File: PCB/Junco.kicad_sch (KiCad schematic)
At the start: 206 parts, among them J1 AudioJack4, J2 AudioJack4, SW1 SW_Push, SW10 SW_Push, SW11 SW_Push, SW12 SW_Push, SW13 SW_Push, SW14 SW_Push, SW15 SW_Push, SW16 SW_Push, SW17 SW_Push, SW18 SW_Push, SW19 SW_MX_Hotswap_Rotary_Switch_R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, SW2 SW_Push, SW20 SW_Push, SW21 SW_Push, SW22 SW_Push, SW23 SW_Push, SW24 SW_Push, SW25 SW_Push, SW26 SW_Push, SW27 SW_Push, SW28 SW_Push, SW29 SW_Push, SW3 SW_Push, SW30 RotaryEncoder_Switch, SW31 SW_Push, SW32 SW_Push, SW33 SW_Push, SW34 SW_Push, SW35 SW_Push, SW36 SW_Push, SW37 SW_Push, SW38 SW_Push, SW39 SW_Push, SW4 SW_Push, SW40 SW_Push, SW41 SW_Push, SW42 SW_Push, SW43 SW_Push, SW44 SW_Push, SW45 SW_Push, SW46 SW_Push, SW47 SW_Push, SW48 SW_Push, SW49 SW_MX_Hotswap_Rotary_Switch_R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, SW5 SW_Push, SW50 SW_Push, SW51 SW_Push, SW52 SW_Push, SW53 SW_Push, SW54 SW_Push, SW55 SW_Push, SW56 SW_Push, SW57 SW_Push, SW58 SW_Push, SW59 SW_Push, SW6 SW_Push, SW60 RotaryEncoder_Switch, SW7 SW_Push, SW8 SW_Push, SW9 SW_Push, U1 Pico, U2 SN74AHCT1G125, U3 Pico, U4 SN74AHCT1G125

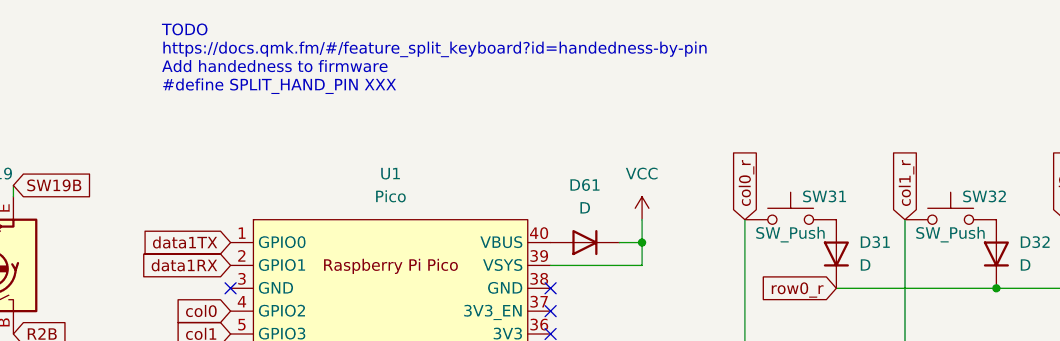
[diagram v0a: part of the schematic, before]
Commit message: Added JLC part number to LED and switch symbols
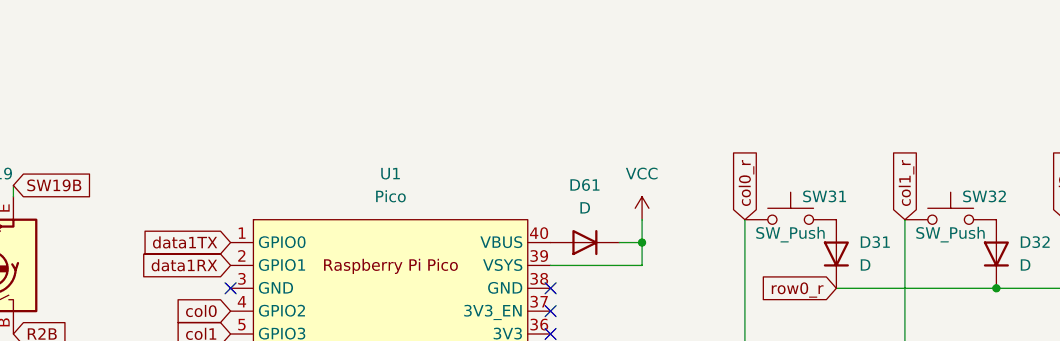
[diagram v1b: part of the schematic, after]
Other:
- note removed: "TODO https://docs.qmk.fm/#/feature_split_keyboard?id=handedness-by-pin Add handedness to firmware #define SPLIT_HAND_PIN XXX"

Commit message: Added level shifter bypass jumper Schematic updated Symbol created and placed
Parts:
- added JP1, JP2: Level shifter bypass jumper, Junco:Level Shifter Bypass Jumper, symbol Jumper:SolderJumper_2_Open
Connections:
- net led: now also JP1.1 (A)
- net led_r: now also JP2.1 (A)
- net at SK68XX_Mini38.4 (DIN), U4.4 (DOUT): now also JP2.2 (B)
- net at SK68XX_Mini1.4 (DIN), U2.4 (DOUT): now also JP1.2 (B)
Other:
- moved on the sheet: SK68XX_Mini1, SK68XX_Mini10, SK68XX_Mini11, SK68XX_Mini12, SK68XX_Mini13, SK68XX_Mini14, SK68XX_Mini15, SK68XX_Mini16, SK68XX_Mini17, SK68XX_Mini18, SK68XX_Mini19, SK68XX_Mini2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

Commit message: Consolidated LED footprints
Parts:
- SK68XX_Mini1, SK68XX_Mini2, SK68XX_Mini3, SK68XX_Mini38, SK68XX_Mini39, SK68XX_Mini4, SK68XX_Mini40, SK68XX_Mini41, SK68XX_Mini42, SK68XX_Mini43, SK68XX_Mini44, SK68XX_Mini45, SK68XX_Mini5, SK68XX_Mini6, SK68XX_Mini7, SK68XX_Mini8: value SK68XXMini -> SK6803MINI-E
- SK68XX_Mini10, SK68XX_Mini11, SK68XX_Mini12, SK68XX_Mini13, SK68XX_Mini14, SK68XX_Mini15, SK68XX_Mini16, SK68XX_Mini17, SK68XX_Mini18, SK68XX_Mini19, SK68XX_Mini20, SK68XX_Mini21, SK68XX_Mini22, SK68XX_Mini23, SK68XX_Mini24, SK68XX_Mini25, SK68XX_Mini26, SK68XX_Mini28, SK68XX_Mini29, SK68XX_Mini30, SK68XX_Mini31, SK68XX_Mini32, SK68XX_Mini33, SK68XX_Mini34, SK68XX_Mini35, SK68XX_Mini36, SK68XX_Mini37, SK68XX_Mini46, SK68XX_Mini47, SK68XX_Mini48, SK68XX_Mini49, SK68XX_Mini50, SK68XX_Mini51, SK68XX_Mini52, SK68XX_Mini53, SK68XX_Mini54, SK68XX_Mini55, SK68XX_Mini56, SK68XX_Mini57, SK68XX_Mini58, SK68XX_Mini59, SK68XX_Mini60, SK68XX_Mini61, SK68XX_Mini62, SK68XX_Mini63, SK68XX_Mini65, SK68XX_Mini66, SK68XX_Mini67, SK68XX_Mini68, SK68XX_Mini69, SK68XX_Mini70, SK68XX_Mini71, SK68XX_Mini72, SK68XX_Mini73, SK68XX_Mini74, SK68XX_Mini9: footprint Junco:SK68XXMini_Offset -> Junco:SK68XXMini
- SK68XX_Mini27: value SK68XXMini_Short_Offset_for_Rotary_Encoder -> SK6803MINI-E; footprint Junco:SK68XXMini_Short_Offset_for_Rotary_Encoder -> Junco:SK68XXMini
- SK68XX_Mini64: value SK68XXMini -> SK6803MINI-E; footprint Junco:SK68XXMini_Short_Offset_for_Rotary_Encoder -> Junco:SK68XXMini
- SW19, SW49: value SW_MX_Hotswap_Rotary_Switch_Rotated -> SW_MX_Hotswap_Rotary_Switch; footprint Junco:SW_MX_Hotswap_Rotary_Switch_Rotated -> Junco:SW_MX_Hotswap_Rotary_Switch

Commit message: Consolidated Switch footprints with 1.5u and 1u
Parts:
- SK68XX_Mini10, SK68XX_Mini11, SK68XX_Mini12, SK68XX_Mini13, SK68XX_Mini14, SK68XX_Mini15, SK68XX_Mini16, SK68XX_Mini17, SK68XX_Mini18, SK68XX_Mini19, SK68XX_Mini20, SK68XX_Mini21, SK68XX_Mini22, SK68XX_Mini23, SK68XX_Mini24, SK68XX_Mini25, SK68XX_Mini26, SK68XX_Mini28, SK68XX_Mini29, SK68XX_Mini30, SK68XX_Mini31, SK68XX_Mini32, SK68XX_Mini33, SK68XX_Mini34, SK68XX_Mini35, SK68XX_Mini36, SK68XX_Mini37, SK68XX_Mini46, SK68XX_Mini47, SK68XX_Mini48, SK68XX_Mini49, SK68XX_Mini50, SK68XX_Mini51, SK68XX_Mini52, SK68XX_Mini53, SK68XX_Mini54, SK68XX_Mini55, SK68XX_Mini56, SK68XX_Mini57, SK68XX_Mini58, SK68XX_Mini59, SK68XX_Mini60, SK68XX_Mini61, SK68XX_Mini62, SK68XX_Mini63, SK68XX_Mini65, SK68XX_Mini66, SK68XX_Mini67, SK68XX_Mini68, SK68XX_Mini69, SK68XX_Mini70, SK68XX_Mini71, SK68XX_Mini72, SK68XX_Mini73, SK68XX_Mini74, SK68XX_Mini9: value SK68XXMini -> SK6803MINI-E
- SW28, SW29, SW58, SW59: footprint marbast_mx:SW_MX_HS_1.5u -> marbast_mx:SW_MX_HS_1u

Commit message: Converted LED outline holes to drill holes tweaked routing for new hole clearance
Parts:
- SK68XX_Mini1, SK68XX_Mini10, SK68XX_Mini11, SK68XX_Mini12, SK68XX_Mini13, SK68XX_Mini14, SK68XX_Mini15, SK68XX_Mini16, SK68XX_Mini17, SK68XX_Mini18, SK68XX_Mini19, SK68XX_Mini2, SK68XX_Mini20, SK68XX_Mini21, SK68XX_Mini22, SK68XX_Mini23, SK68XX_Mini24, SK68XX_Mini25, SK68XX_Mini26, SK68XX_Mini27, SK68XX_Mini28, SK68XX_Mini29, SK68XX_Mini3, SK68XX_Mini30, SK68XX_Mini31, SK68XX_Mini32, SK68XX_Mini33, SK68XX_Mini34, SK68XX_Mini35, SK68XX_Mini36, SK68XX_Mini37, SK68XX_Mini38, SK68XX_Mini39, SK68XX_Mini4, SK68XX_Mini40, SK68XX_Mini41, SK68XX_Mini42, SK68XX_Mini43, SK68XX_Mini44, SK68XX_Mini45, SK68XX_Mini46, SK68XX_Mini47, SK68XX_Mini48, SK68XX_Mini49, SK68XX_Mini5, SK68XX_Mini50, SK68XX_Mini51, SK68XX_Mini52, SK68XX_Mini53, SK68XX_Mini54, SK68XX_Mini55, SK68XX_Mini56, SK68XX_Mini57, SK68XX_Mini58, SK68XX_Mini59, SK68XX_Mini6, SK68XX_Mini60, SK68XX_Mini61, SK68XX_Mini62, SK68XX_Mini63, SK68XX_Mini64, SK68XX_Mini65, SK68XX_Mini66, SK68XX_Mini67, SK68XX_Mini68, SK68XX_Mini69, SK68XX_Mini7, SK68XX_Mini70, SK68XX_Mini71, SK68XX_Mini72, SK68XX_Mini73, SK68XX_Mini74, SK68XX_Mini8, SK68XX_Mini9: footprint Junco:SK68XXMini -> Junco:SK68XXMini_drill_hole_mod
